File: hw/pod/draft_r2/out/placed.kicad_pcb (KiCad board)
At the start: 4 copper layers, 30 x 12 mm, 74 parts, among them J1 TestPoint_Pad_D1.0mm, J10 TestPoint_Pad_D1.0mm, J11 TestPoint_Pad_D1.0mm, J12 TestPoint_Pad_D1.0mm, J2 TestPoint_Pad_D1.0mm, J3 TestPoint_Pad_D1.0mm, J4 WirePad_1.0x2.0mm, J5 TestPoint_Pad_D1.0mm, J7 TestPoint_Pad_D1.0mm, J8 TestPoint_Pad_D1.0mm, J9 TestPoint_Pad_D1.0mm, Q1 Nexperia_SOT1216_DFN1010B-6, Q2 Nexperia_SOT1216_DFN1010B-6, SW1 SW-SMD_4P-L3.0-W2.6-P1.85-LS3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, U1 QFN-48-1EP_7x7mm_P0.5mm_EP5.6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, U2 Knowles_LGA-5_3.5x2.65mm, U3 DSBGA-8_L1.6-W0.9-R2-C4-P0.40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, U4 X2SON-4_L1.0-W1.0-P0.65-TL-EP, U6 SOT-553-5_L1.6-W1.2-P0.50-LS1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, Y1 Crystal_SMD_2012-2Pin_2.0x1.2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

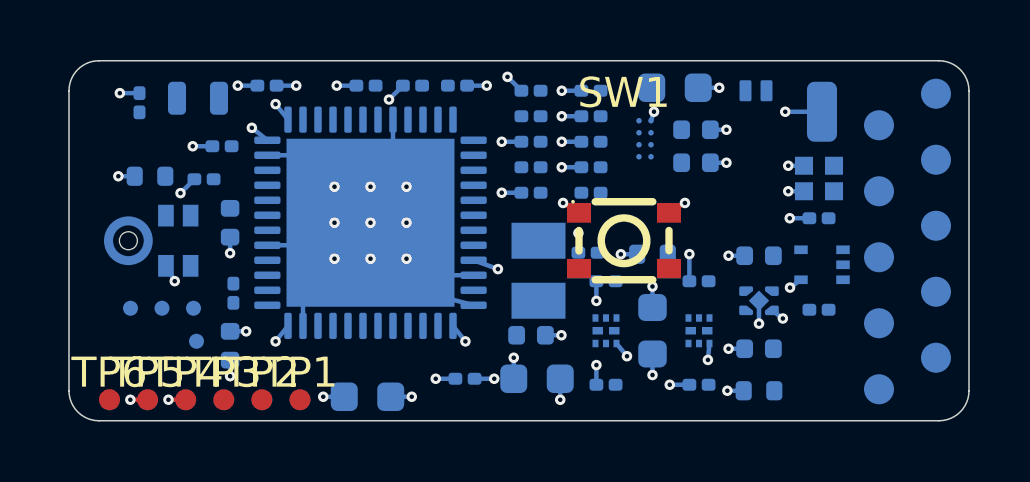
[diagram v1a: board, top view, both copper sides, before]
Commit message: Phase 2 route closure (agent v6): 1 unconnected (I2C_SCL at U1.26), DRC 0 errors, placement check pass: U1 top strip loosened (C2/C3/C10), C9 pocket fixed, Y1 vertical, TP3/TP6 moved on F; mic port now x 1.88 (shell_r2 re-check)
Co-Authored-By: Claude Opus 5.5 <noreply@anthropic.com>
Claude-Session: https://claude.ai/code/session_01Wg997D6KFs8bxoAH56jZZJ
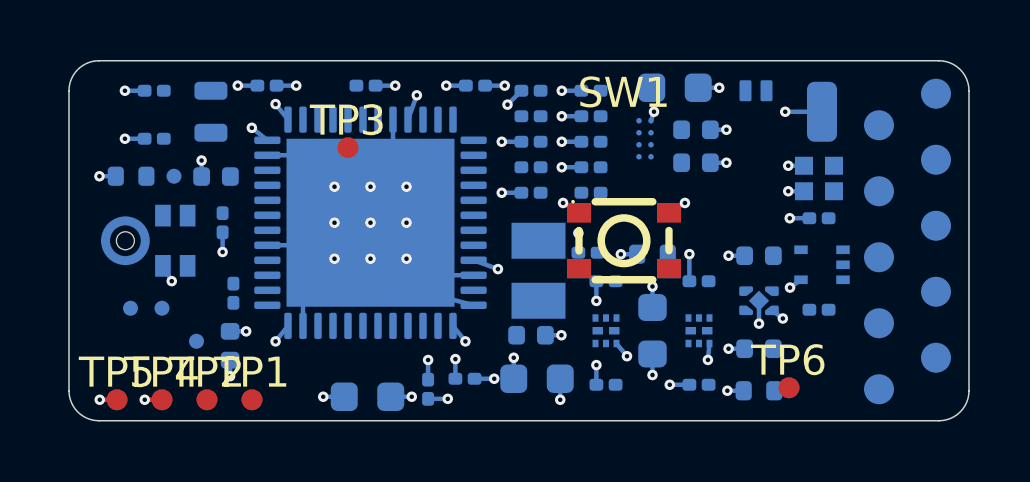
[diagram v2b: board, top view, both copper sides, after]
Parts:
- moved TP6 22.7 mm to (24.0, 10.9)
- moved C2 10.1 mm to (12.0, 10.9), turned to -90 degrees
- moved TP3 9.36 mm to (9.30, 2.90)
- moved TP8 4.45 mm to (3.50, 3.85)
- moved C11 2.27 mm to (2.84, 2.60)
- moved TP2 1.83 mm to (4.60, 11.3)
- moved C9 1.61 mm to (4.90, 3.86), turned to 180 degrees
- moved TP1 1.60 mm to (6.10, 11.3)
- moved C13 1.58 mm to (5.12, 5.40), turned to -90 degrees
- moved TP5 1.02 mm to (1.60, 11.3)
- moved TP4 0.79 mm to (3.10, 11.3)
- moved C12 0.63 mm to (2.84, 1.00), turned to 180 degrees
- moved R1 0.63 mm to (2.07, 3.85)
- moved Y1 0.62 mm to (4.73, 1.70), turned to 90 degrees
- moved C3 0.60 mm to (13.6, 0.83)
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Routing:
- net +3V0: track 13.5 -> 15.7 mm, vias 21 -> 24

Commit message: Phase-2 board: B-DOC-AUDIT-0007 layout fixes 1-3 (local re-route of the committed board)
- J3 DOCK_VBUS / J4 GND swapped: J4 now sits between J3 and J5 VBAT (ASM-09); J3-J5 gap 1.17 -> 2.80 mm, all wire-pad gaps >= 0.90
- mic-port keep-out (R-ACO-P6): F.Cu rule area r 1.6 in place_r2 (FreeRouting + DRC enforce it), fan-out avoids it, check 'port';
  MDF_SDI re-routed: nearest F copper / via 1.35 -> 1.87 mm from the port
- LSE: Y1/C11/C12 moved, C1 to the QFN corner; LSE_IN/LSE_OUT pre-routed on B (locked), 0 vias, 7.72 / 7.43 mm (was 2 vias each, F+B)
- VDDA pin 9: C6 100 nF at the pin (1.13 mm, was 8.8), C5 1 uF 2.32 mm (was 9.2); C3 to VDD pin 36; C10 / R9 nudged; NEAR rules per pin
- R21 stays mid-board (MZD-4 not done): edge position scored LN-M03 2.48 % (limit 2) or an unroutable BRIDGE_RTN when flipped
- tools: place_r2 pre-routes / keep-out / --probe / --fr-args; local_reroute.py (move + rip + locked FreeRouting pass);
  fb_bridge.py (F+B maze, rip-and-repair); inner_bridge F/B layers + pads/rule areas as obstacles; kelvin_r21 reads the R21 pad
- DRC 0 / 0 unconnected; place_r2 check pass; LN M01..M05 26.5 / 20.1 / 1.29 % / 0.127 / 8.72 (unchanged); smoke exit 0

Co-Authored-By: Claude Opus 5.5 <noreply@anthropic.com>
Claude-Session: https://claude.ai/code/session_01Wg997D6KFs8bxoAH56jZZJ
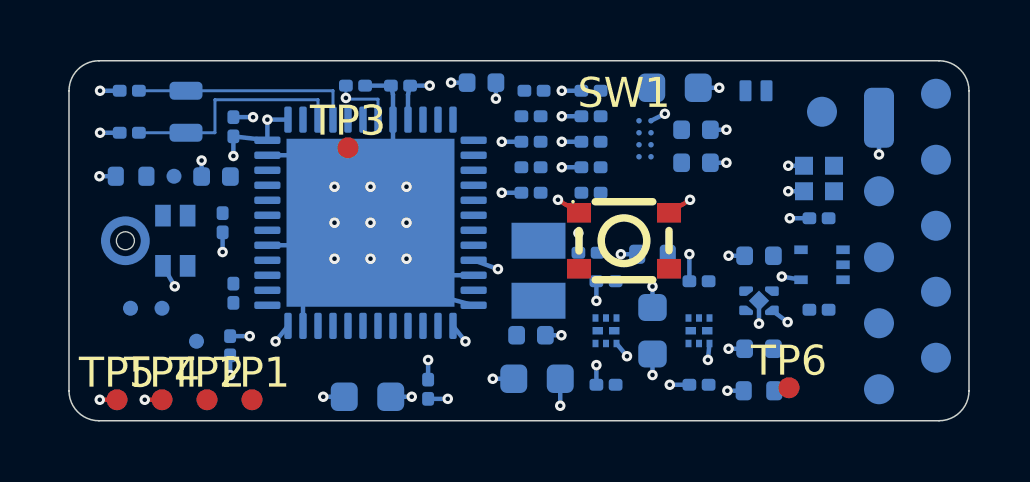
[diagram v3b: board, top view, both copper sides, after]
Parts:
- moved C5 12.1 mm to (13.8, 0.73), turned to 0 degrees
- moved C3 11.9 mm to (5.37, 9.50), turned to 90 degrees
- moved C6 10.0 mm to (11.1, 0.83)
- moved J3 1.95 mm to (25.1, 1.70)
- moved J4 1.91 mm to (27.0, 1.90)
- moved C1 1.77 mm to (5.48, 2.20), turned to 90 degrees
- moved C11 0.85 mm to (2.01, 2.40)
- moved C12 0.83 mm to (2.01, 1.00)
- moved Y1 0.83 mm to (3.90, 1.70)
- moved C10 0.35 mm to (9.55, 0.83)
- moved R9 0.10 mm to (15.5, 1.00)
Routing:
- net LSE_IN: track 0.00 -> 7.73 mm
- net LSE_OUT: track 0.00 -> 7.43 mm
- net NRST: track 0.00 -> 2.20 mm, vias 0 -> 1
- net +3V0: track 15.7 -> 17.6 mm, vias 24 -> 22
- net GND: track 30.1 -> 31.1 mm, vias 48 -> 45
